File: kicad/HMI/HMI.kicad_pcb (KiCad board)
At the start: 2 copper layers, 45 parts, among them J2 SWD, J3 DEM 128128A TMH-PW-N, J4 RIBBON, SW1 SW_Push, SW10 SW_Push, SW11 SW_Push, SW12 SW_Push, SW13 SW_Push, SW14 SW_Push, SW15 SW_Push, SW16 SW_Push, SW17 SW_Push, SW18 SW_Push, SW19 SW_Push, SW2 SW_Push, SW20 SW_Push, SW3 SW_Push, SW4 SW_Push, SW5 SW_Push, SW6 SW_Push, SW7 SW_Push, SW8 SW_Push, SW9 SW_Push, U1 STM32L011K4Tx, X1 ASV-4.000MHZ-EJ-T

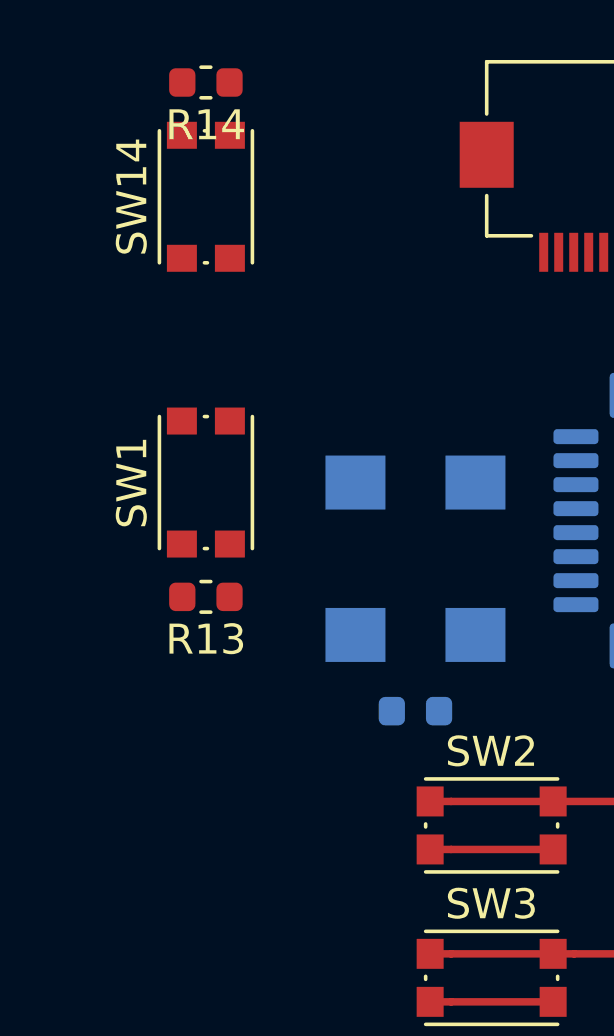
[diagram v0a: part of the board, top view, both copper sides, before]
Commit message: HMI - changed SW1 and SW14 button footprint; Mainboard - further changes; TR-9 library, correcting footprint
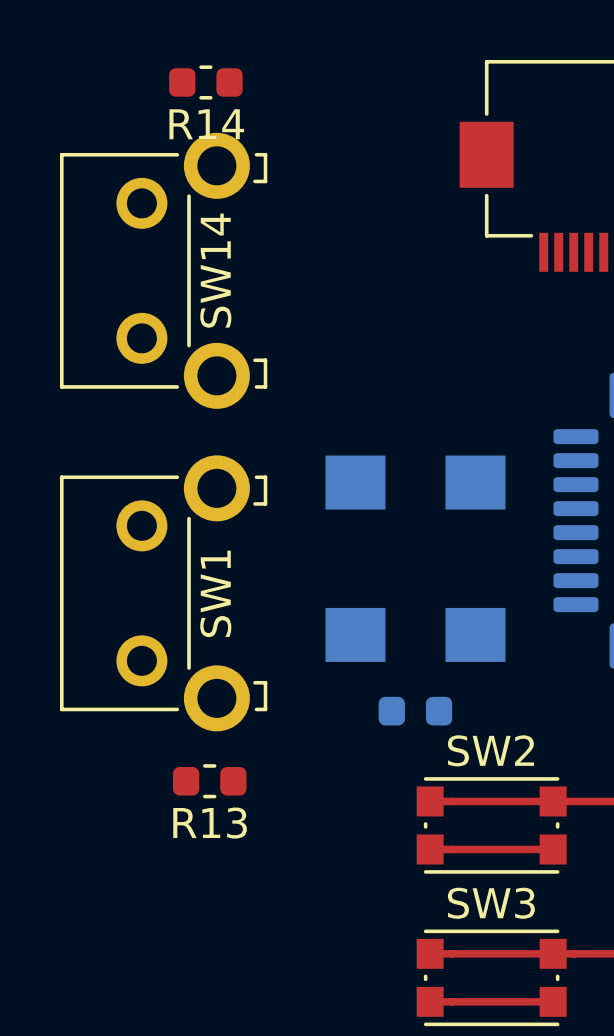
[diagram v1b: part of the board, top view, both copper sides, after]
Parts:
- SW1, SW14: footprint Button_Switch_SMD:SW_Push_1P1T_NO_CK_KMR2 -> Button_Switch_THT:SW_Tactile_SKHH_Angled
- moved SW1 6.31 mm to (73.4, 77.7)
- moved R13 6.15 mm to (75.7, 81.7)
- moved SW14 5.18 mm to (73.4, 66.9)

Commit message: HMI: added design of PCB -> plotted PDF -> plotted production output - Gerbers -> HMI is READY!!
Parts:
- added C9: 1u, Capacitor_SMD:C_0603_1608Metric, B.Cu at (93.8, 67.5)
- C6, J3, R13, R14, R5, R6: moved to B.Cu
- moved C2 83.2 mm to (75.2, 99.0), turned to 270 degrees
- moved C4 83.0 mm to (75.2, 104.4), turned to 270 degrees
- moved C7 81.6 mm to (77.4, 106.6), turned to 180 degrees
- moved C5 80.9 mm to (77.4, 103.7)
- moved C3 80.9 mm to (77.4, 98.2)
- moved C8 80.5 mm to (77.4, 101.2), turned to 180 degrees
- moved FB1 78.8 mm to (77.4, 105.2), turned to 180 degrees
- moved FB2 78.2 mm to (77.4, 99.7), turned to 180 degrees
- moved J2 33.5 mm to (73.0, 57.5), turned to 180 degrees
- moved C1 17.4 mm to (99.6, 76.0), turned to 0 degrees
- moved X1 17.0 mm to (99.3, 71.5), turned to 270 degrees
- moved C6 15.2 mm to (83.1, 76.3), turned to 270 degrees
- moved J4 12.4 mm to (79.1, 102.7)
- moved R5 11.0 mm to (95.1, 71.7)
- moved R6 8.40 mm to (102.4, 59.3)
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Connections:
- J3 pad 16: GND -> SPI1_CS
- J3 pad 17: GND -> SPI1_SCK
- J3 pad 18: SPI1_MOSI -> +3V3
- J3 pad 19: GND -> +3V3
- J3 pad 2: Net-(J3-Pad2) -> GND
- J3 pad 20: TFT_RST -> +5V
- J3 pad 21: GND -> Net-(J3-Pad21)
- J3 pad 3: +5V -> TFT_RST
- J3 pad 4: +3V3 -> GND
- J3 pad 5: +3V3 -> SPI1_MOSI
- J3 pad 6: SPI1_SCK -> GND
- J3 pad 7: SPI1_CS -> GND
- R6 pad 2: Net-(J3-Pad2) -> Net-(J3-Pad21)
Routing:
- net +3V3: track 30.7 -> 159.1 mm, vias 0 -> 5
- net SPI1_CS: track 0.00 -> 80.4 mm, vias 0 -> 2
- net SPI1_MOSI: track 0.00 -> 79.9 mm
- net TFT_RST: track 0.00 -> 76.2 mm
- net SPI1_SCK: track 0.00 -> 76.1 mm
- net TX: track 0.00 -> 75.7 mm, vias 0 -> 2
- net TFT_LED: track 0.00 -> 73.2 mm
- net +5V: track 0.00 -> 68.2 mm, vias 0 -> 1
- net C1: track 24.6 -> 68.8 mm, vias 0 -> 13
- net C2: track 24.6 -> 65.8 mm, vias 0 -> 13
- net C3: track 24.6 -> 62.7 mm, vias 0 -> 11
- net R1: track 19.8 -> 54.2 mm, vias 0 -> 3
- net NRST: track 0.00 -> 32.6 mm, vias 0 -> 2
- net R2: track 19.8 -> 49.9 mm, vias 0 -> 4
- net R3: track 19.8 -> 44.0 mm, vias 0 -> 1
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- added copper zone on B.Cu, net GND
- added copper zone on F.Cu, net GND
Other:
- board outline added: 37 x 72.8 mm
- rule via_min_drill: 0.3 -> 0.2
- board text added: "1"
